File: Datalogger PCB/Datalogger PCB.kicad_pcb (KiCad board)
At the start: 4 copper layers, 42.2 x 101.8 mm, 46 parts, among them J1 Conn_01x02_Pin, M1 Motor_Servo, M2 Motor_Servo, M3 Motor_Servo, M4 Motor_Servo, U1 Teensy4.1, U2 BNO055, U3 LPS25HB, U4 AMS1117-5.0, U5 NRF24L01_Breakout, U6 VN5E160STR-E, U7 VN5E160STR-E, U8 VN5E160STR-E, U9 VN5E160STR-E

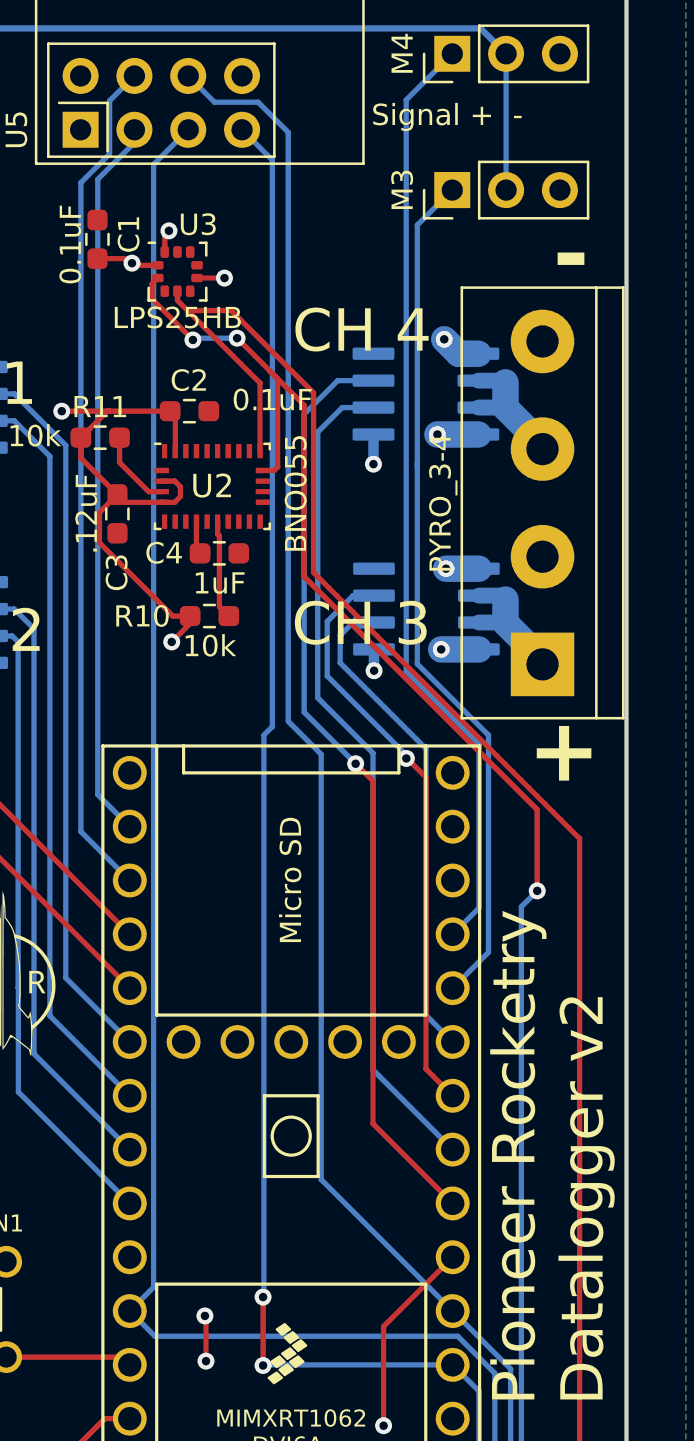
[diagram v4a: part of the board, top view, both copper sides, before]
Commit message: Added pull down resistor to pyro channels
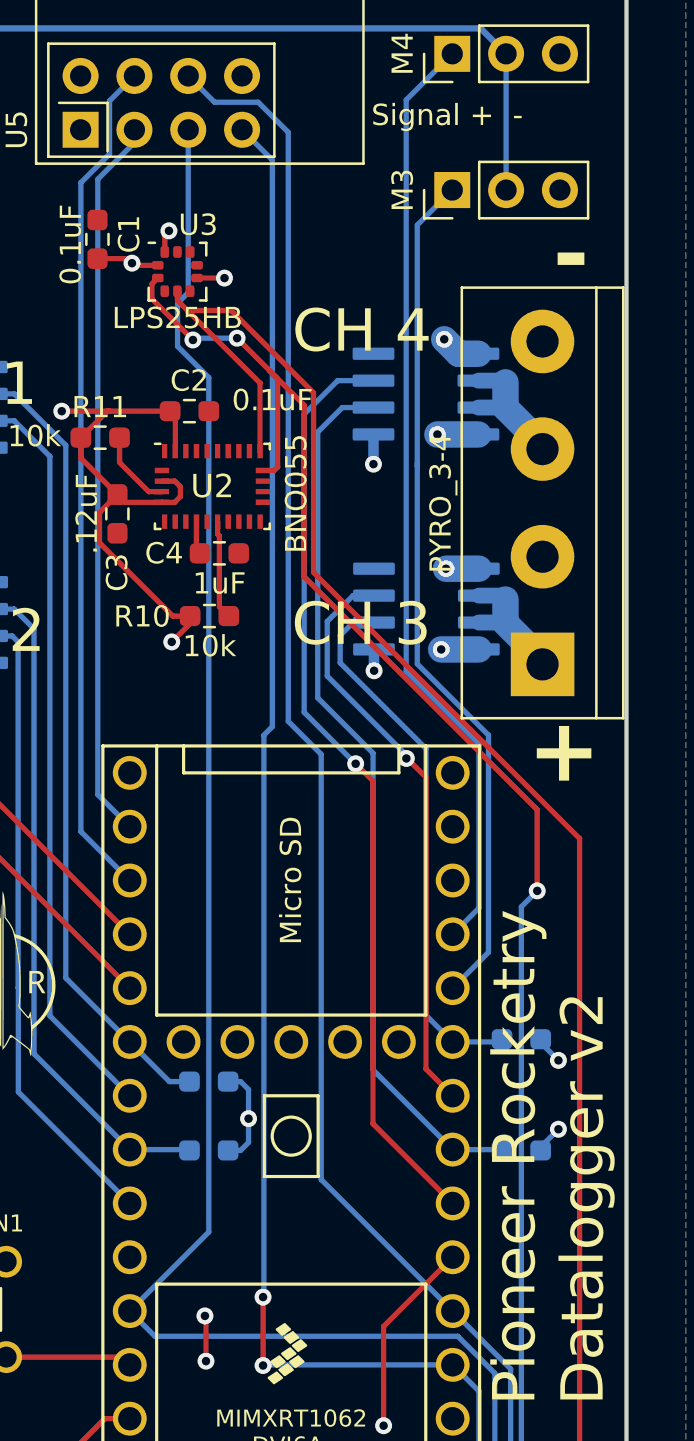
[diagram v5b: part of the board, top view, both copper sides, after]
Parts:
- added R14: 10k, Resistor_SMD:R_0603_1608Metric_Pad0.98x0.95mm_HandSolder, B.Cu at (174.8, 95.5)
- added R15: 10k, Resistor_SMD:R_0603_1608Metric_Pad0.98x0.95mm_HandSolder, B.Cu at (174.8, 100.8)
- added R4: 10k, Resistor_SMD:R_0603_1608Metric_Pad0.98x0.95mm_HandSolder, B.Cu at (160.0, 100.8)
- added R5: 10k, Resistor_SMD:R_0603_1608Metric_Pad0.98x0.95mm_HandSolder, B.Cu at (160.0, 97.5)
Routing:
- net GND: track 15.8 -> 23.2 mm, vias 6 -> 9
- net /PYRO_1: track 34.1 -> 37.7 mm
- net /PYRO_2: track 29.0 -> 31.9 mm
- net /PYRO_3: track 23.2 -> 25.6 mm
- net /PYRO_4: track 39.6 -> 42.0 mm
- net /CLK: track 92.4 -> 93.6 mm

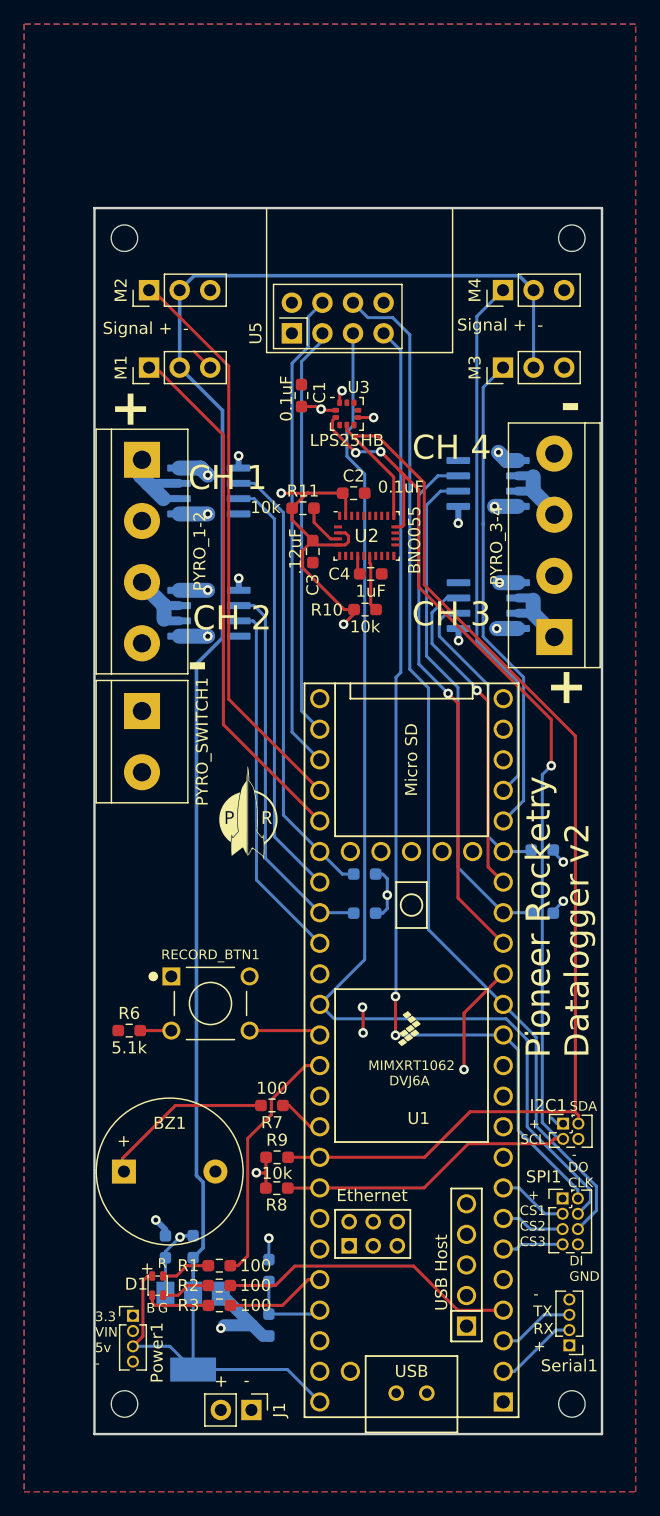
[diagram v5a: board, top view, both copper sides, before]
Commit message: Fixed a couple of pcb errors
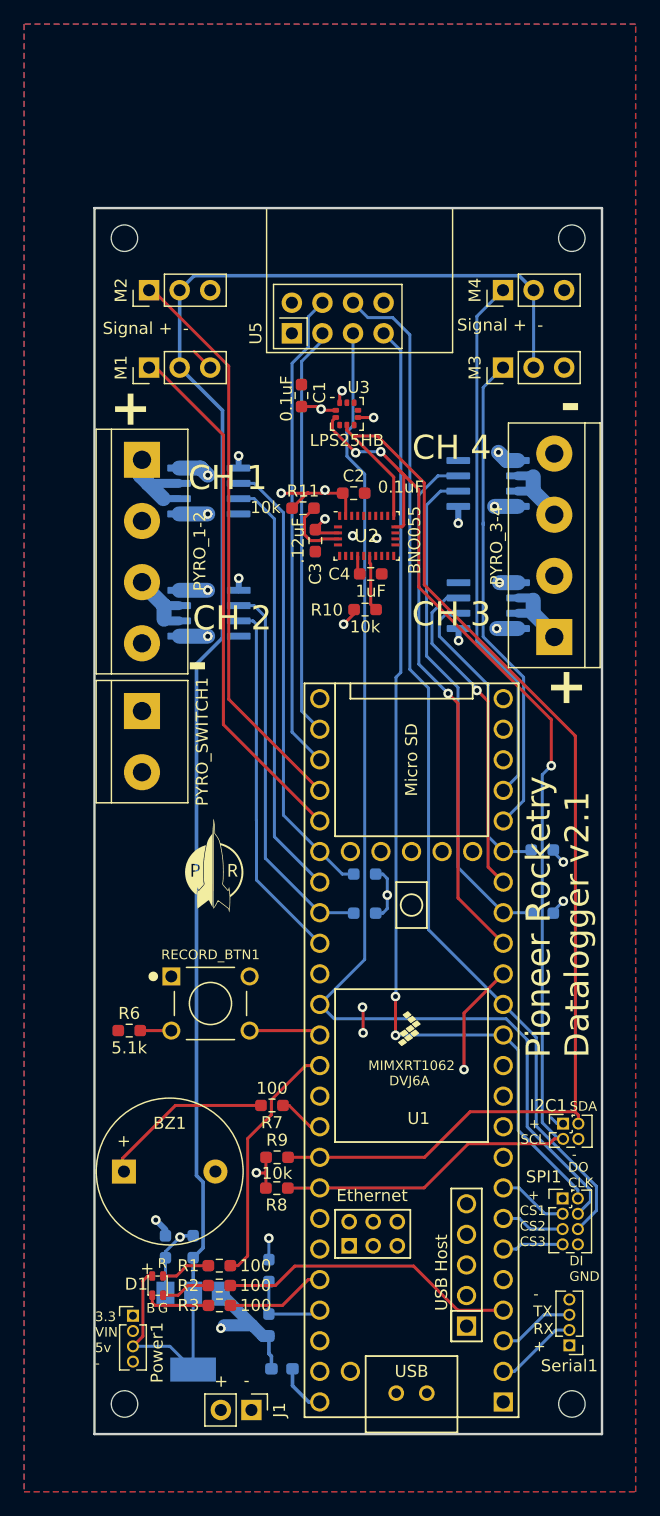
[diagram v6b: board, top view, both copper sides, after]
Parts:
- added D2: D, Diode_SMD:D_0603_1608Metric_Pad1.05x0.95mm_HandSolder, B.Cu at (153.1, 138.6)
- moved G*** 5.22 mm to (147.4, 96.6)
- moved C3 0.94 mm to (155.9, 69.8)
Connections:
- U1 pad 48: +5V -> Net-(D2-A)
- U2 pad 5: +3.3V -> GND
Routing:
- net +3.3V: track 48.8 -> 35.8 mm, vias 9 -> 11
- net +5V: track 153.4 -> 141.7 mm
- net Net-(D2-A): track 0.00 -> 4.23 mm
- net /VIN: track 74.7 -> 77.5 mm
- net Net-(U2-~{BOOT_LOAD_PIN}): track 3.74 -> 5.56 mm
- net GND: vias 9 -> 11
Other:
- board text added: "Pioneer Rocketry Datalogger v2.1"
- board text removed: "Pioneer Rocketry Datalogger v2"

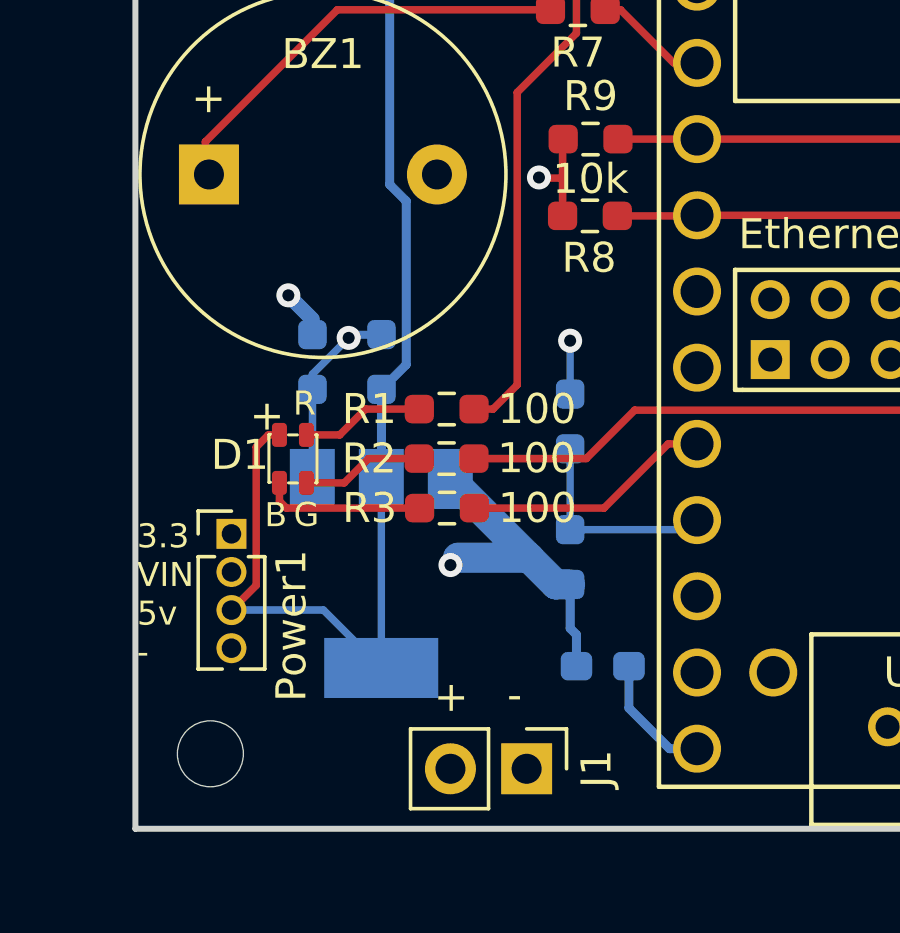
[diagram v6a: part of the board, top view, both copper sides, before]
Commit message: Modified the 5v power rail a little
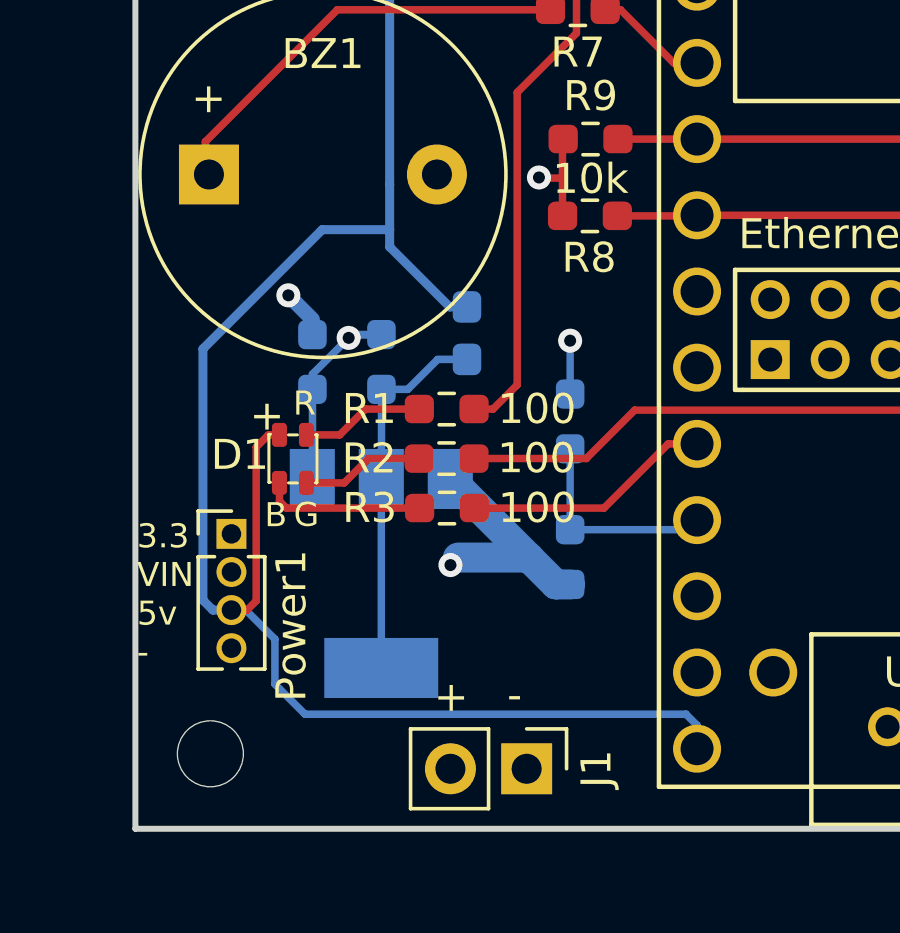
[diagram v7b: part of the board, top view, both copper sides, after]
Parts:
- moved D2 12.0 mm to (148.6, 127.5), turned to -90 degrees
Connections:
- C6 pad 2: +5V -> Net-(D2-A)
- D2 pad 1: /VIN -> +5V
- U1 pad 48: Net-(D2-A) -> +5V
- U4 pad 2: +5V -> Net-(D2-A)
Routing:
- net +5V: track 141.7 -> 161.4 mm
- net Net-(D2-A): track 4.23 -> 13.0 mm
- net /VIN: track 77.5 -> 74.7 mm
